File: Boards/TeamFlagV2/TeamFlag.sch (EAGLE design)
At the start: 7 parts

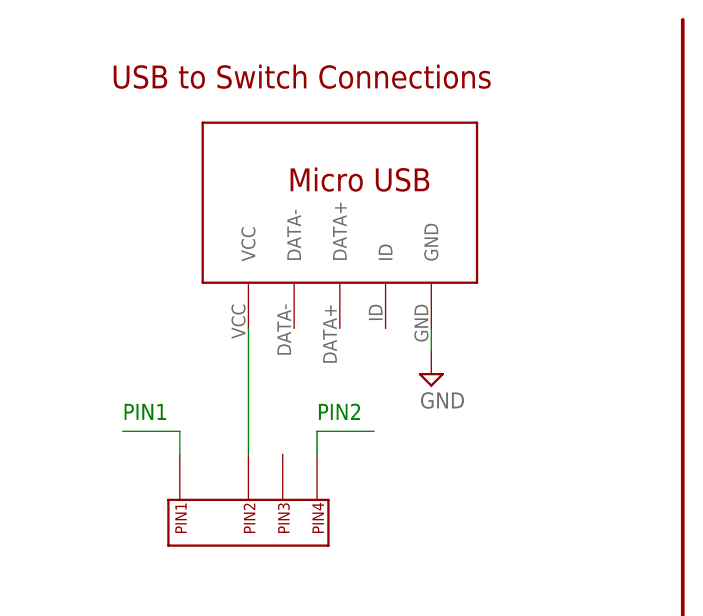
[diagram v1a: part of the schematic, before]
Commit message: team flag fixed <3 margo
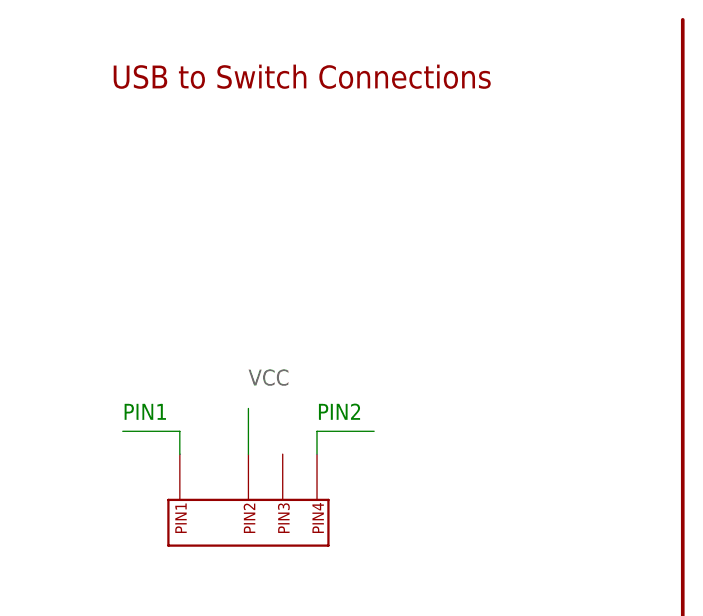
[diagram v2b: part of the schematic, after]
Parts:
- removed U$1: MICRO_USB, pie:MICRO_USB
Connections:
- net GND: no longer U$1.GND
- net VCC: no longer U$1.VCC
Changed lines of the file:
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@@
 <?xml version="1.0" encoding="utf-8"?>
 <!DOCTYPE eagle SYSTEM "eagle.dtd">
-<eagle version="8.0.0">
+<eagle version="8.2.2">
 <drawing>
 <settings>
@@
 <attribute name="REVISION" value="10A"/>
 </part>
-<part name="U$1" library="pie" deviceset="MICRO_USB" device=""/>
 <part name="LED1" library="pie" deviceset="LED" device="LED5MM-NOFLAT" value="Yellow"/>
 <part name="LED2" library="pie" deviceset="LED" device="LED5MM-NOFLAT" value="Blue"/>
 <part name="R1" library="pie" deviceset="R-US_" device="R0603" value="130"/>
 <part name="R2" library="pie" deviceset="R-US_" device="R0603" value="130"/>
-<part name="SUPPLY1" library="pie" deviceset="GND" device=""/>
 <part name="SUPPLY2" library="pie" deviceset="GND" device=""/>
 <part name="C1" library="pie" deviceset="CAP" device="0603-CAP" value="0.1uF"/>
@@
 </instance>
 <instance part="FRAME1" gate="G$2" x="147.32" y="0"/>
-<instance part="U$1" gate="G$1" x="22.86" y="151.13"/>
 <instance part="LED1" gate="G$1" x="41.91" y="96.52"/>
 <instance part="LED2" gate="G$1" x="43.18" y="82.55"/>
 <instance part="R1" gate="G$1" x="26.67" y="96.52" rot="R180"/>
 <instance part="R2" gate="G$1" x="27.94" y="82.55" rot="R180"/>
-<instance part="SUPPLY1" gate="GND" x="45.72" y="146.05"/>
 <instance part="SUPPLY2" gate="GND" x="52.07" y="76.2"/>
 <instance part="C1" gate="G$1" x="34.29" y="25.4" rot="R90"/>
@@
 </segment>
 <segment>
-<pinref part="U$1" gate="G$1" pin="GND"/>
-<pinref part="SUPPLY1" gate="GND" pin="GND"/>
-<wire x1="45.72" y1="151.13" x2="45.72" y2="148.59" width="0.1524" layer="91"/>
-</segment>
-<segment>
 <pinref part="C1" gate="G$1" pin="1"/>
 <pinref part="SUPPLY3" gate="GND" pin="GND"/>
@@
 <segment>
 <pinref part="U$2" gate="G$1" pin="PIN2"/>
-<pinref part="U$1" gate="G$1" pin="VCC"/>
-<wire x1="25.4" y1="137.16" x2="25.4" y2="151.13" width="0.1524" layer="91"/>
-</segment>
-</net>
+<wire x1="25.4" y1="137.16" x2="25.4" y2="142.24" width="0.1524" layer="91"/>
+<label x="25.4" y="144.78" size="1.778" layer="91" font="vector" ratio="6"/>
+</segment>
+</net>

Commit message: team flag screw terminal
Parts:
- added ST1: 2PIN_SCREW, pie:2PIN_SCREW
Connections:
- net GND: now also ST1.P$2
- net VCC: now also ST1.P$1
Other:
- note added: "2-pin Screw Terminal"
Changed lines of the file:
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@@
 <?xml version="1.0" encoding="utf-8"?>
 <!DOCTYPE eagle SYSTEM "eagle.dtd">
-<eagle version="8.3.2">
+<eagle version="9.4.2">
 <drawing>
 <settings>
@@
 <layer number="59" name="tCarbon" color="7" fill="1" visible="no" active="no"/>
 <layer number="60" name="bCarbon" color="7" fill="1" visible="no" active="no"/>
+<layer number="88" name="SimResults" color="9" fill="1" visible="yes" active="yes"/>
+<layer number="89" name="SimProbes" color="9" fill="1" visible="yes" active="yes"/>
 <layer number="90" name="Modules" color="5" fill="1" visible="yes" active="yes"/>
 <layer number="91" name="Nets" color="2" fill="1" visible="yes" active="yes"/>
@@
 <layer number="113" name="IDFDebug" color="7" fill="1" visible="yes" active="yes"/>
 <layer number="114" name="Badge_Outline" color="11" fill="1" visible="no" active="no"/>
+<layer number="115" name="ReferenceISLANDS" color="7" fill="1" visible="yes" active="yes"/>
 <layer number="116" name="Patch_BOT" color="9" fill="4" visible="yes" active="yes"/>
+<layer number="117" name="BACKMAAT1" color="7" fill="1" visible="yes" active="yes"/>
 <layer number="118" name="Rect_Pads" color="7" fill="1" visible="yes" active="yes"/>
+<layer number="119" name="KAP_TEKEN" color="7" fill="1" visible="yes" active="yes"/>
+<layer number="120" name="KAP_MAAT1" color="7" fill="1" visible="yes" active="yes"/>
 <layer number="121" name="_tsilk" color="7" fill="1" visible="yes" active="yes"/>
 <layer number="122" name="_bsilk" color="7" fill="1" visible="yes" active="yes"/>
@@
 <layer number="128" name="_bValues" color="7" fill="1" visible="yes" active="yes"/>
 <layer number="129" name="Mask" color="7" fill="1" visible="yes" active="yes"/>
+<layer number="130" name="SMDSTROOK" color="7" fill="1" visible="yes" active="yes"/>
 <layer number="131" name="tAdjust" color="7" fill="1" visible="yes" active="yes"/>
 <layer number="132" name="bAdjust" color="7" fill="1" visible="yes" active="yes"/>
+<layer number="133" name="BGA_CORE_SUP" color="12" fill="1" visible="yes" active="yes"/>
+<layer number="134" name="BGA_GND" color="1" fill="1" visible="yes" active="yes"/>
+<layer number="135" name="BGA_NC" color="8" fill="1" visible="yes" active="yes"/>
+<layer number="136" name="BGA_DED" color="14" fill="1" visible="yes" active="yes"/>
+<layer number="137" name="mtTest" color="7" fill="1" visible="yes" active="yes"/>
+<layer number="138" name="mbTest" color="7" fill="1" visible="yes" active="yes"/>
+<layer number="139" name="mtKeepout" color="7" fill="1" visible="yes" active="yes"/>
+<layer number="140" name="mbKeepout" color="7" fill="1" visible="yes" active="yes"/>
+<layer number="141" name="mtRestrict" color="7" fill="1" visible="yes" active="yes"/>
+<layer number="142" name="mbRestrict" color="7" fill="1" visible="yes" active="yes"/>
+<layer number="143" name="mvRestrict" color="7" fill="1" visible="yes" active="yes"/>
 <layer number="144" name="Drill_legend" color="7" fill="1" visible="yes" active="yes"/>
+<layer number="145" name="mHoles" color="7" fill="1" visible="yes" active="yes"/>
+<layer number="146" name="mMilling" color="7" fill="1" visible="yes" active="yes"/>
+<layer number="147" name="mMeasures" color="7" fill="1" visible="yes" active="yes"/>
+<layer number="148" name="mDocument" color="7" fill="1" visible="yes" active="yes"/>
+<layer number="149" name="mReference" color="7" fill="1" visible="yes" active="yes"/>
 <layer number="150" name="Notes" color="7" fill="1" visible="yes" active="yes"/>
 <layer number="151" name="HeatSink" color="7" fill="1" visible="yes" active="yes"/>
@@
 <layer number="154" name="FabDoc2" color="7" fill="1" visible="yes" active="yes"/>
 <layer number="155" name="FabDoc3" color="7" fill="1" visible="yes" active="yes"/>
+<layer number="191" name="mNets" color="7" fill="1" visible="yes" active="yes"/>
+<layer number="192" name="mBusses" color="7" fill="1" visible="yes" active="yes"/>
+<layer number="193" name="mPins" color="7" fill="1" visible="yes" active="yes"/>
+<layer number="194" name="mSymbols" color="7" fill="1" visible="yes" active="yes"/>
+<layer number="195" name="mNames" color="7" fill="1" visible="yes" active="yes"/>
+<layer number="196" name="mValues" color="7" fill="1" visible="yes" active="yes"/>
 <layer number="199" name="Contour" color="7" fill="1" visible="yes" active="yes"/>
 <layer number="200" name="200bmp" color="1" fill="10" visible="yes" active="yes"/>
@@
 <layer number="230" name="230bmp" color="7" fill="1" visible="yes" active="yes"/>
 <layer number="231" name="231bmp" color="7" fill="1" visible="yes" active="yes"/>
+<layer number="232" name="Eagle3D_PG2" color="7" fill="1" visible="yes" active="yes"/>
+<layer number="233" name="Eagle3D_PG3" color="7" fill="1" visible="yes" active="yes"/>
 <layer number="248" name="Housing" color="7" fill="1" visible="yes" active="yes"/>
 <layer number="249" name="Edge" color="7" fill="1" visible="yes" active="yes"/>
@@
 <part name="SUPPLY3" library="pie" deviceset="GND" device=""/>
 <part name="U$2" library="pie" deviceset="SP3T_SLIDE_SWITCH" device=""/>
+<part name="ST1" library="pie" deviceset="2PIN_SCREW" device=""/>
 </parts>
 <sheets>
@@
 <text x="10.16" y="177.8" size="2.54" layer="94" font="vector">USB to Switch Connections</text>
 <text x="22.86" y="109.22" size="2.54" layer="94" font="vector">LED Circuits</text>
-<text x="15.24" y="50.8" size="2.54" layer="94" font="vector">Decoupling Capacitor</text>
+<text x="17.78" y="50.8" size="2.54" layer="94" font="vector">Decoupling Capacitor</text>
+<text x="96.52" y="101.6" size="2.54" layer="94" font="vector">2-pin Screw Terminal</text>
 </plain>
 <instances>
-<instance part="FRAME1" gate="G$1" x="0" y="0">
+<instance part="FRAME1" gate="G$1" x="0" y="0" smashed="yes">
 <attribute name="AUTHOR" x="0" y="0" size="1.778" layer="96" display="off"/>
 <attribute name="REVISION" x="0" y="0" size="1.778" layer="96" display="off"/>
 </instance>
-<instance part="FRAME1" gate="G$2" x="147.32" y="0"/>
-<instance part="LED1" gate="G$1" x="41.91" y="96.52"/>
-<instance part="LED2" gate="G$1" x="43.18" y="82.55"/>
-<instance part="R1" gate="G$1" x="26.67" y="96.52" rot="R180"/>
-<instance part="R2" gate="G$1" x="27.94" y="82.55" rot="R180"/>
-<instance part="SUPPLY2" gate="GND" x="52.07" y="76.2"/>
-<instance part="C1" gate="G$1" x="34.29" y="25.4" rot="R90"/>
-<instance part="SUPPLY3" gate="GND" x="34.29" y="15.24"/>
-<instance part="U$2" gate="G$1" x="16.51" y="127"/>
+<instance part="FRAME1" gate="G$2" x="147.32" y="0" smashed="yes">
+<attribute name="LAST_DATE_TIME" x="160.02" y="1.27" size="2.54" layer="94" font="vector"/>
+<attribute name="SHEET" x="233.68" y="1.27" size="2.54" layer="94" font="vector"/>
+<attribute name="DRAWING_NAME" x="162.814" y="17.78" size="2.7432" layer="94" font="vector"/>
+<attribute name="AUTHOR" x="148.59" y="6.985" size="2.7432" layer="94" font="vector"/>
+<attribute name="REVISION" x="236.22" y="6.985" size="2.7432" layer="94" font="vector"/>
+</instance>
+<instance part="LED1" gate="G$1" x="41.91" y="96.52" smashed="yes">
+<attribute name="NAME" x="38.1" y="99.06" size="1.778" layer="95"/>
+<attribute name="VALUE" x="38.1" y="90.17" size="1.778" layer="96"/>
+</instance>
+<instance part="LED2" gate="G$1" x="43.18" y="82.55" smashed="yes">
+<attribute name="NAME" x="39.37" y="85.09" size="1.778" layer="95"/>
+<attribute name="VALUE" x="39.37" y="76.2" size="1.778" layer="96"/>
+</instance>
+<instance part="R1" gate="G$1" x="26.67" y="96.52" smashed="yes" rot="R180">
+<attribute name="NAME" x="31.75" y="93.98" size="1.778" layer="95" rot="R180"/>
+<attribute name="VALUE" x="31.75" y="100.33" size="1.778" layer="96" rot="R180"/>
+</instance>
+<instance part="R2" gate="G$1" x="27.94" y="82.55" smashed="yes" rot="R180">
+<attribute name="NAME" x="33.02" y="80.01" size="1.778" layer="95" rot="R180"/>
+<attribute name="VALUE" x="33.02" y="86.36" size="1.778" layer="96" rot="R180"/>
+</instance>
+<instance part="SUPPLY2" gate="GND" x="52.07" y="76.2" smashed="yes">
+<attribute name="VALUE" x="50.8" y="72.39" size="1.778" layer="96"/>
+</instance>
+<instance part="C1" gate="G$1" x="34.29" y="25.4" smashed="yes" rot="R90">
+<attribute name="NAME" x="31.75" y="21.59" size="1.778" layer="95" rot="R90"/>
+<attribute name="VALUE" x="39.37" y="21.59" size="1.778" layer="96" rot="R90"/>
+</instance>
+<instance part="SUPPLY3" gate="GND" x="34.29" y="15.24" smashed="yes">
+<attribute name="VALUE" x="33.02" y="11.43" size="1.778" layer="96"/>
+</instance>
+<instance part="U$2" gate="G$1" x="16.51" y="127" smashed="yes"/>
+<instance part="ST1" gate="G$1" x="116.84" y="78.74" smashed="yes">
+<attribute name="NAME" x="111.76" y="88.9" size="2.54" layer="94"/>
+</instance>
 </instances>
 <busses>
@@
 <wire x1="34.29" y1="22.86" x2="34.29" y2="17.78" width="0.1524" layer="91"/>
 </segment>
+<segment>
+<pinref part="ST1" gate="G$1" pin="P$2"/>
+<wire x1="104.14" y1="76.2" x2="99.06" y2="76.2" width="0.1524" layer="91"/>
+<label x="93.98" y="76.2" size="1.778" layer="95"/>
+</segment>
 </net>
 <net name="N$2" class="0">
@@
 <label x="25.4" y="144.78" size="1.778" layer="91" font="vector" ratio="6"/>
 </segment>
+<segment>
+<pinref part="ST1" gate="G$1" pin="P$1"/>
+<wire x1="104.14" y1="81.28" x2="99.06" y2="81.28" width="0.1524" layer="91"/>
+<label x="93.98" y="81.28" size="1.778" layer="95"/>
+</segment>
 </net>

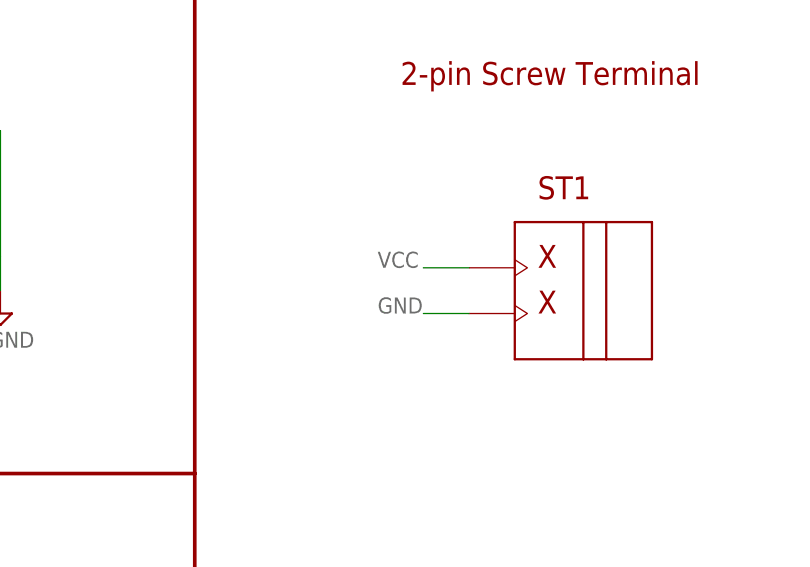
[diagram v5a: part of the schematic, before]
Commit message: Generated gerbers for production
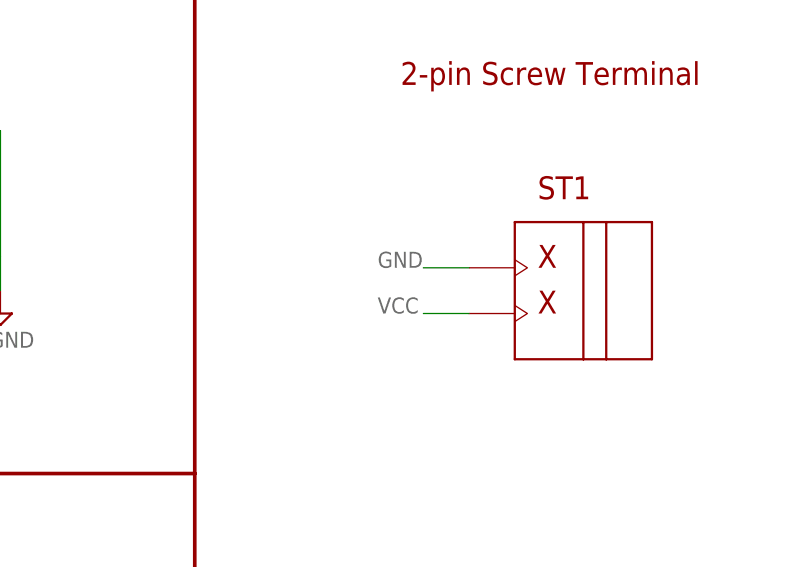
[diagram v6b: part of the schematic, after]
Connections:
- net GND: now also ST1.P$1; no longer ST1.P$2
- net VCC: now also ST1.P$2; no longer ST1.P$1
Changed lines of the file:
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@@
 </segment>
 <segment>
-<pinref part="ST1" gate="G$1" pin="P$2"/>
-<wire x1="104.14" y1="76.2" x2="99.06" y2="76.2" width="0.1524" layer="91"/>
-<label x="93.98" y="76.2" size="1.778" layer="95"/>
+<pinref part="ST1" gate="G$1" pin="P$1"/>
+<wire x1="104.14" y1="81.28" x2="99.06" y2="81.28" width="0.1524" layer="91"/>
+<label x="93.98" y="81.28" size="1.778" layer="95"/>
 </segment>
 </net>
@@
 </segment>
 <segment>
-<pinref part="ST1" gate="G$1" pin="P$1"/>
-<wire x1="104.14" y1="81.28" x2="99.06" y2="81.28" width="0.1524" layer="91"/>
-<label x="93.98" y="81.28" size="1.778" layer="95"/>
+<pinref part="ST1" gate="G$1" pin="P$2"/>
+<wire x1="104.14" y1="76.2" x2="99.06" y2="76.2" width="0.1524" layer="91"/>
+<label x="93.98" y="76.2" size="1.778" layer="95"/>
 </segment>
 </net>
